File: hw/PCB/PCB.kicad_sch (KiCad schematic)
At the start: 208 parts, among them IC1 SN74HC251PWR, IC2 SN74LV138APWR, IC3 SN74HC251PWR, K1 KEYSW, K10 KEYSW, K11 KEYSW, K12 KEYSW, K13 KEYSW, K14 KEYSW, K16 KEYSW, K17 KEYSW, K18 KEYSW, K19 KEYSW, K2 KEYSW, K20 KEYSW, K21 KEYSW, K22 KEYSW, K23 KEYSW, K24 KEYSW, K25 KEYSW, K26 KEYSW, K27 KEYSW, K28 KEYSW, K29 KEYSW, K3 KEYSW, K31 KEYSW, K32 KEYSW, K33 KEYSW, K34 KEYSW, K35 KEYSW, K36 KEYSW, K37 KEYSW, K38 KEYSW, K39 KEYSW, K4 KEYSW, K40 KEYSW, K41 KEYSW, K42 KEYSW, K43 KEYSW, K44 KEYSW, K46 KEYSW, K47 KEYSW, K48 KEYSW, K49 KEYSW, K5 KEYSW, K50 KEYSW, K51 KEYSW, K52 KEYSW, K53 KEYSW, K54 KEYSW, K55 KEYSW, K56 KEYSW, K57 KEYSW, K58 KEYSW, K59 KEYSW, K6 KEYSW, K61 KEYSW, K62 KEYSW, K63 KEYSW, K64 KEYSW, K65 KEYSW, K66 KEYSW, K67 KEYSW, K68 KEYSW, K69 KEYSW, K7 KEYSW, K8 KEYSW, K9 KEYSW, U1 TXB0108DQSR, U6 STM32L552ZETxQ

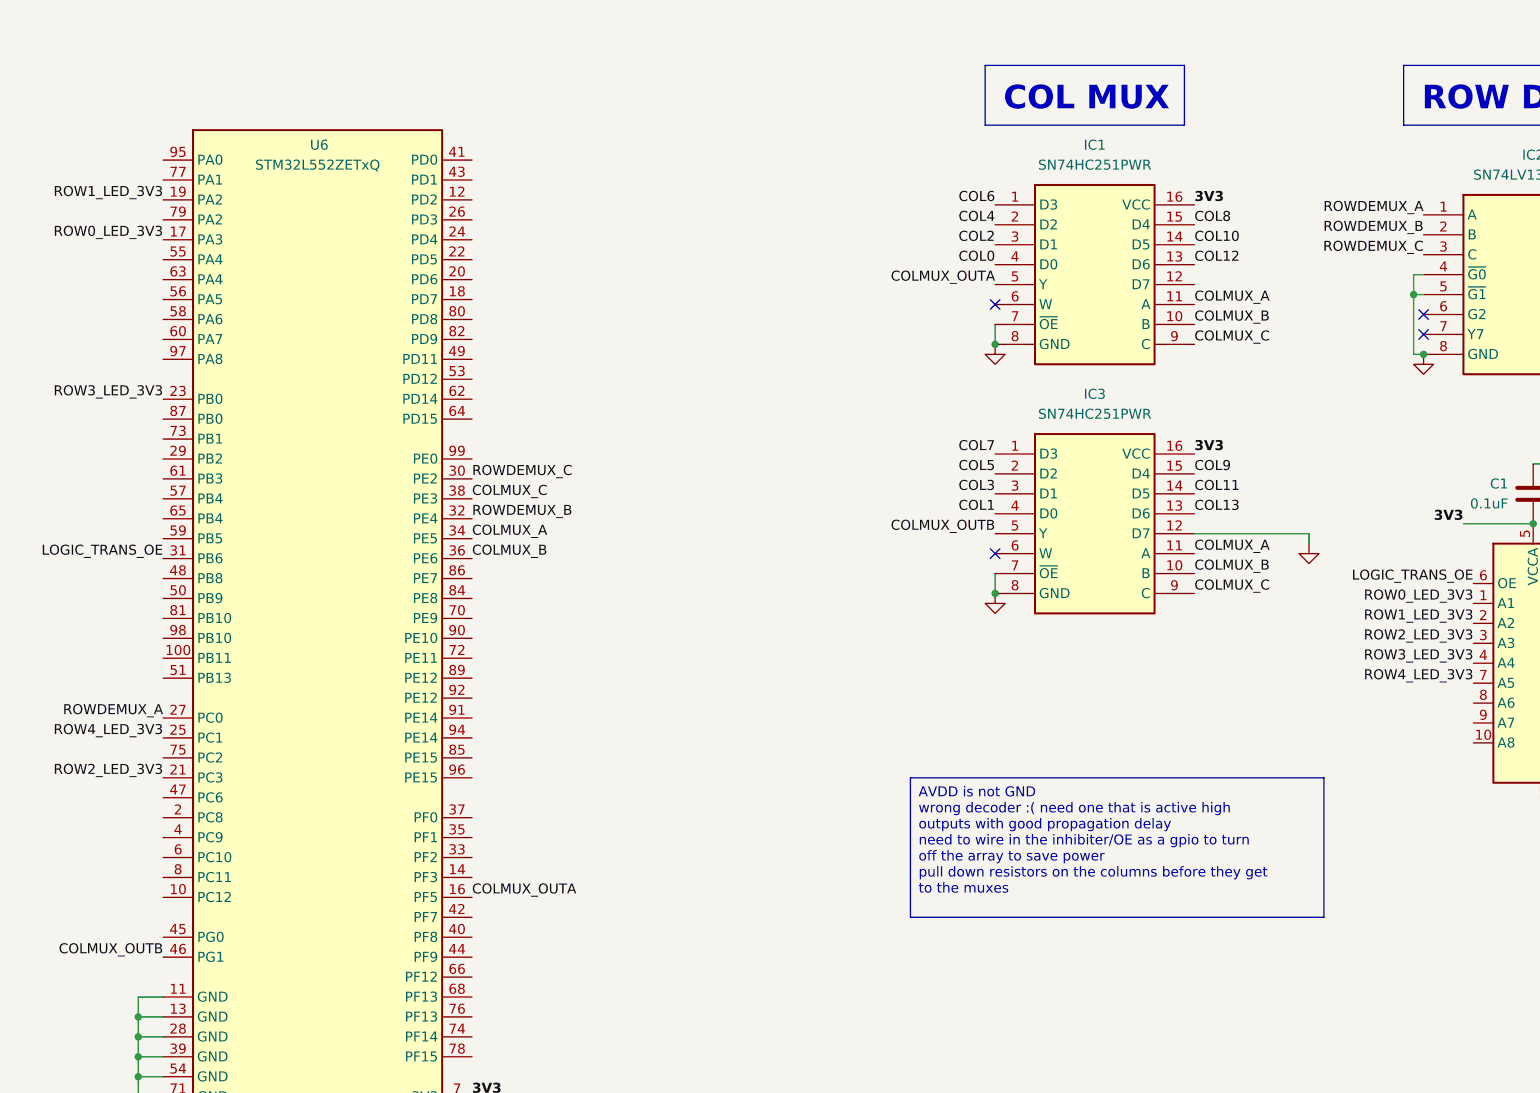
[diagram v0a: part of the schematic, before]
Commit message: The LEDs work!!
LEDs use DMA PWM to generate their bit encoding scheme
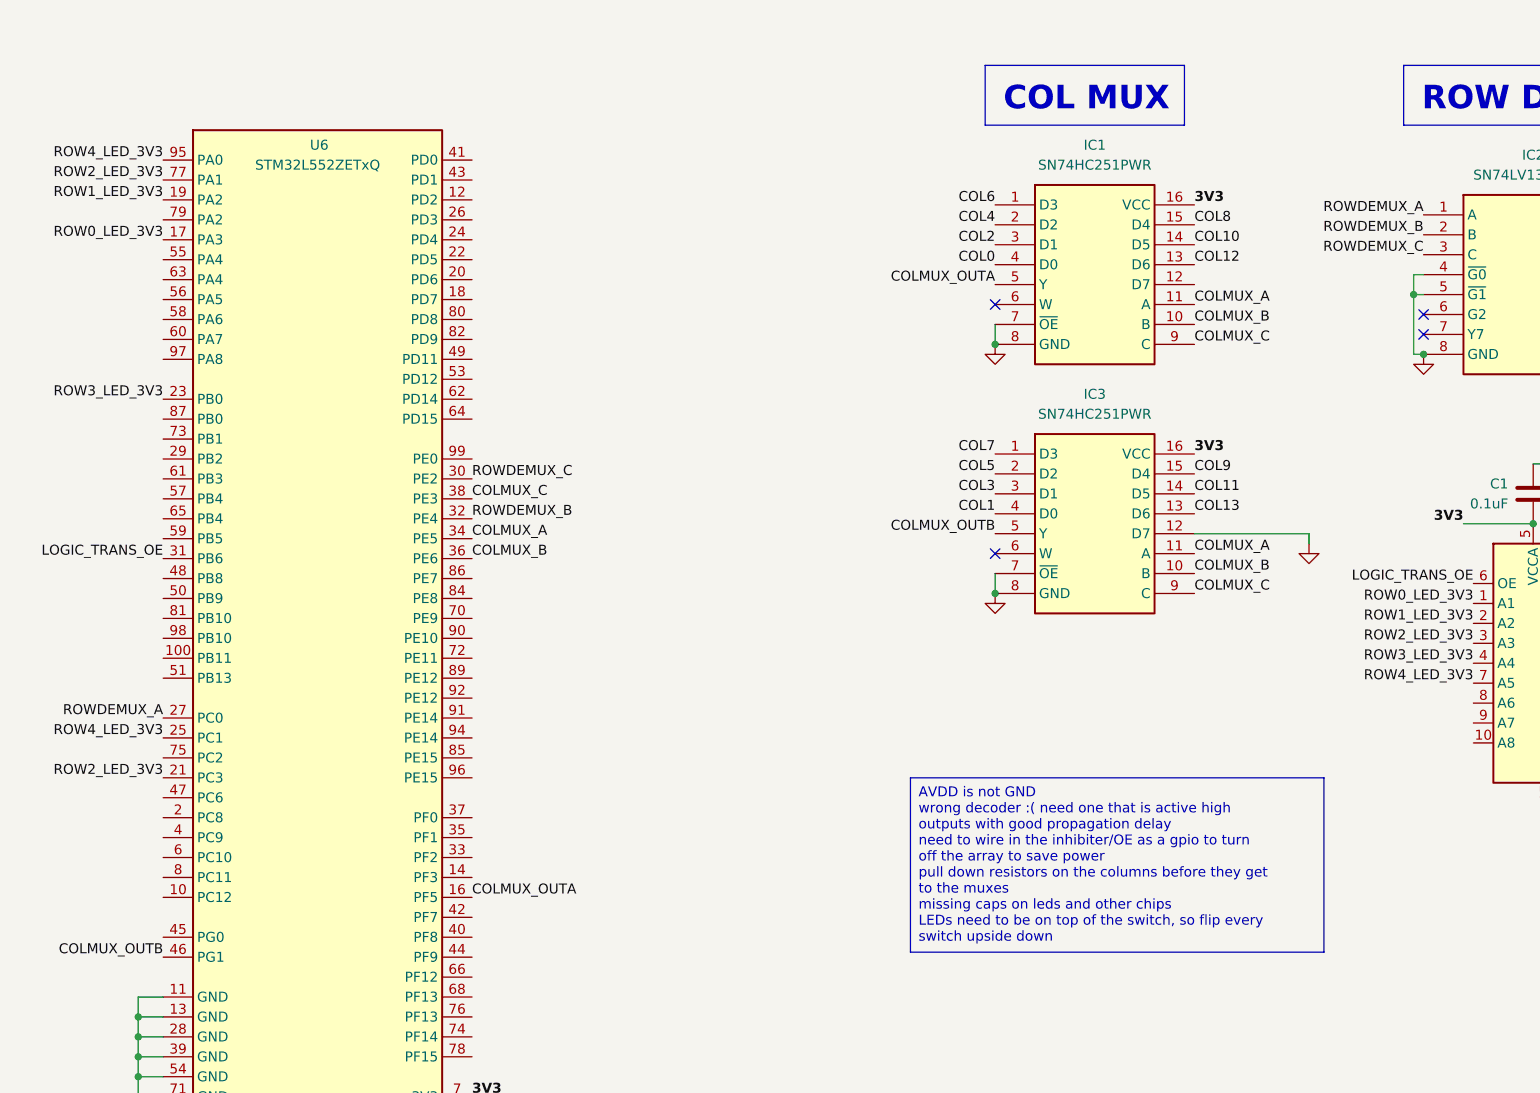
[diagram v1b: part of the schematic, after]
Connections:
- net ROW2_LED_3V3: now also U6.77 (PA1)
- net ROW4_LED_3V3: now also U6.95 (PA0)
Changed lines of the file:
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@@
     (effects (font (size 5 5) (thickness 0.254) bold (color 0 4 255 1)) (justify left top))
   )
-  (text_box "AVDD is not GND\nwrong decoder :( need one that is active high outputs with good propagation delay\nneed to wire in the inhibiter/OE as a gpio to turn off the array to save power\npull down resistors on the columns before they get to the muxes"
-    (at 156.21 182.245 0) (size 52.705 17.78)
+  (text_box "AVDD is not GND\nwrong decoder :( need one that is active high outputs with good propagation delay\nneed to wire in the inhibiter/OE as a gpio to turn off the array to save power\npull down resistors on the columns before they get to the muxes\nmissing caps on leds and other chips\nLEDs need to be on top of the switch, so flip every switch upside down"
+    (at 156.21 182.245 0) (size 52.705 22.225)
     (stroke (width 0) (type default))
     (fill (type none))
@@
     (effects (font (size 1.27 1.27)) (justify right bottom))
   )
+  (label "ROW4_LED_3V3" (at 60.96 103.505 180) (fields_autoplaced)
+    (effects (font (size 1.27 1.27)) (justify right bottom))
+  )
   (label "COL4" (at 167.005 111.76 180) (fields_autoplaced)
     (effects (font (size 1.27 1.27)) (justify right bottom))
@@
     (effects (font (size 1.27 1.27)) (justify left bottom))
   )
+  (label "ROW2_LED_3V3" (at 60.96 106.045 180) (fields_autoplaced)
+    (effects (font (size 1.27 1.27)) (justify right bottom))
+  )
   (label "ROW2_LED_3V3" (at 60.96 182.245 180) (fields_autoplaced)

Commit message: Schematic Updates
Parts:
- removed IC1: SN74HC251PWR, SN74HC251PWR:SOP65P640X120-16N, symbol SN74HC251PWR:SN74HC251PWR
- removed IC2: SN74LV138APWR, SN74LV138APWR:SOP65P640X120-16N, symbol SN74LV138APWR:SN74LV138APWR
- removed IC3: SN74HC251PWR, SN74LV138APWR:SOP65P640X120-16N, symbol SN74HC251PWR:SN74HC251PWR
- removed JP1, JP2, JP3, JP4, JP5, JP6: SolderJumper_2_Bridged, Jumper:SolderJumper-2_P1.3mm_Bridged_RoundedPad1.0x1.5mm, symbol Jumper:SolderJumper_2_Bridged
- removed LED69: WS2812B, Keebio-Parts.pretty-master:SK6812-MINI-E, symbol LED:WS2812B
- removed U1: TXB0108DQSR, Package_SON:USON-20_2x4mm_P0.4mm, symbol Logic_LevelTranslator:TXB0108DQSR
- removed U6: STM32L552ZETxQ, STZio:STZio, symbol STZio:STM32L552ZETxQ_Zio
- added 1: ~, symbol PCB-altium-import:root_0_Battery_pack_NTC
- added 1: ~, symbol PCB-altium-import:root_0_nPM1300_QEAA
- added C10, C12, C19, C20, C21, C22, C23, C24, C25, C26, C27, C28, C29, C3, C30, C31, C32, C33, C34, C35, C36, C37, C38, C39, C4, C40, C41, C42, C43, C44, C45, C46, C47, C48, C49, C5, C50, C51, C52, C53, C54, C55, C56, C57, C58, C59, C6, C60, C61, C62, C63, C64, C65, C66, C67, C68, C69, C7, C70, C71, C72, C73, C74, C8, C9: 100nF, symbol Device:C
- added C11: 2.2uF, symbol Device:C
- added C13: 1uF, symbol Device:C
- added C16: 10uF, symbol Device:C
- added D15: D, Diode_SMD:D_SOD-123, symbol Device:D
- added D30: PRTR5V0U2X, Package_TO_SOT_SMD:SOT-143, symbol Power_Protection:PRTR5V0U2X
- added J1: USB_C_Receptacle_USB2.0, Connector_USB:USB3_A_Molex_48393-001, symbol Connector:USB_C_Receptacle_USB2.0
- added J2: Adafruit TFT, symbol Connector_Generic:Conn_01x11
- added K15: KEYSW, MX_Hotswap:MX-Hotswap-1.25U, symbol keyboard_parts:KEYSW
- added L0603G: ~, symbol Device:LED
- added L0603R, L0603Y: LED, symbol Device:LED
- added L1, L2: 2.2uH, symbol Device:L
- added LED15, LED30: WS2812B, Keebio-Parts.pretty-master:SK6812-MINI-E, symbol LED:WS2812B
- added R1: 47K, symbol Device:R
- added R2: 250K, symbol Device:R
- added SW1: SW_Push, symbol Switch:SW_Push
- added U1: nRF52840, Package_DFN_QFN:Nordic_AQFN-73-1EP_7x7mm_P0.5mm, symbol MCU_Nordic:nRF52840
- added U2: MS88SF2, MS88SF2:XCVR_MS88SF2, symbol MS88SF2:MS88SF2
- added U3, U4: 74HC595, symbol 74xx:74HC595
- C1, C2: value 0.1uF -> 100nF; footprint Capacitor_SMD:C_0603_1608Metric_Pad1.08x0.95mm_HandSolder -> (none)
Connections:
- net 3V3 is gone; now on net GND: C1.2
- net ROW1_LED_5V is gone; now on an unnamed net: LED29.4 (DIN)
- net ROW2_LED_5V is gone; now on an unnamed net: LED44.4 (DIN)
- net 5V: now also C1.1, C2.1, LED1.1 (VDD), LED10.1 (VDD), LED11.1 (VDD), LED12.1 (VDD), LED13.1 (VDD), LED14.1 (VDD), LED16.1 (VDD), LED17.1 (VDD), LED18.1 (VDD), LED19.1 (VDD), LED2.1 (VDD), LED20.1 (VDD), LED21.1 (VDD), LED22.1 (VDD), LED23.1 (VDD), LED24.1 (VDD), LED25.1 (VDD), LED26.1 (VDD), LED27.1 (VDD), LED28.1 (VDD), LED29.1 (VDD), LED3.1 (VDD), LED31.1 (VDD), LED32.1 (VDD), LED33.1 (VDD), LED34.1 (VDD), LED35.1 (VDD), LED36.1 (VDD), LED37.1 (VDD), LED38.1 (VDD), LED39.1 (VDD), LED4.1 (VDD), LED40.1 (VDD), LED41.1 (VDD), LED42.1 (VDD), LED43.1 (VDD), LED44.1 (VDD), LED46.1 (VDD), LED47.1 (VDD), LED48.1 (VDD), LED49.1 (VDD), LED5.1 (VDD), LED50.1 (VDD), LED51.1 (VDD), LED52.1 (VDD), LED53.1 (VDD), LED54.1 (VDD), LED55.1 (VDD), LED56.1 (VDD), LED57.1 (VDD), LED58.1 (VDD), LED59.1 (VDD), LED6.1 (VDD), LED61.1 (VDD), LED62.1 (VDD), LED63.1 (VDD), LED64.1 (VDD), LED65.1 (VDD), LED66.1 (VDD), LED67.1 (VDD), LED68.1 (VDD), LED7.1 (VDD), LED8.1 (VDD), LED9.1 (VDD), C10.1, C19.1, C20.1, C21.1, C22.1, C23.1, C24.1, C25.1, C26.1, C27.1, C28.1, C29.1, C3.1, C30.1, C31.1, C32.1, C33.1, C34.1, C35.1, C36.1, C37.1, C38.1, C39.1, C4.1, C40.1, C41.1, C42.1, C43.1, C44.1, C45.1, C46.1, C47.1, C48.1, C49.1, C5.1, C50.1, C51.1, C52.1, C53.1, C54.1, C55.1, C56.1, C57.1, C58.1, C59.1, C6.1, C60.1, C61.1, C62.1, C63.1, C64.1, C65.1, C66.1, C67.1, C68.1, C69.1, C7.1, C70.1, C71.1, C72.1, C73.1, C74.1, C8.1, C9.1, LED15.1 (VDD), LED30.1 (VDD)
- net COL0: now also U3.15 (QA)
- net COL1: now also U3.1 (QB)
- net COL10: now also U4.2 (QC)
- net COL11: now also U4.3 (QD)
- net COL12: now also U4.4 (QE)
- net COL13: now also U4.5 (QF)
- net COL2: now also U3.2 (QC)
- net COL3: now also U3.3 (QD)
- net COL4: now also U3.4 (QE)
- net COL5: now also U3.5 (QF)
- net COL6: now also U3.6 (QG)
- net COL7: now also U3.7 (QH)
- net COL8: now also K15.1, U4.15 (QA)
- net COL9: now also U4.1 (QB)
- net GND: now also C2.2, 1.2 (PVSS1), 1.28 (LSIN1/VINLDO1), 1.29 (LSOUT1/VOUTLDO1), 1.30 (LSIN2/VINLDO2), 1.31 (LSOUT2/VOUTLDO2), 1.33 (AVSS), 1.6 (PVSS2), C10.2, C11.1, C12.2, C13.2, C16.2, C19.2, C20.2, C21.2, C22.2, C23.2, C24.2, C25.2, C26.2, C27.2, C28.2, C29.2, C3.2, C30.2, C31.2, C32.2, C33.2, C34.2, C35.2, C36.2, C37.2, C38.2, C39.2, C4.2, C40.2, C41.2, C42.2, C43.2, C44.2, C45.2, C46.2, C47.2, C48.2, C49.2, C5.2, C50.2, C51.2, C52.2, C53.2, C54.2, C55.2, C56.2, C57.2, C58.2, C59.2, C6.2, C60.2, C61.2, C62.2, C63.2, C64.2, C65.2, C66.2, C67.2, C68.2, C69.2, C7.2, C70.2, C71.2, C72.2, C73.2, C74.2, C8.2, C9.2, D30.1 (GND), J1.A1 (GND), J1.A12 (GND), J1.B1 (GND), J1.B12 (GND), J1.S1 (SHIELD), J2.3 (Pin_3), LED15.3 (VSS), LED30.3 (VSS), R1.2, R2.2, SW1.1, U3.13 (~{OE}), U4.13 (~{OE}); no longer C1.1, C2.1
- net ROW0: now also D1.1 (K), D10.1 (K), D11.1 (K), D12.1 (K), D13.1 (K), D14.1 (K), D2.1 (K), D3.1 (K), D4.1 (K), D5.1 (K), D6.1 (K), D7.1 (K), D8.1 (K), D9.1 (K); no longer D1.2 (A), D10.2 (A), D11.2 (A), D12.2 (A), D13.2 (A), D14.2 (A), D2.2 (A), D3.2 (A), D4.2 (A), D5.2 (A), D6.2 (A), D7.2 (A), D8.2 (A), D9.2 (A)
- net ROW1: now also D16.1 (K), D17.1 (K), D18.1 (K), D19.1 (K), D20.1 (K), D21.1 (K), D22.1 (K), D23.1 (K), D24.1 (K), D25.1 (K), D26.1 (K), D27.1 (K), D28.1 (K), D29.1 (K); no longer D16.2 (A), D17.2 (A), D18.2 (A), D19.2 (A), D20.2 (A), D21.2 (A), D22.2 (A), D23.2 (A), D24.2 (A), D25.2 (A), D26.2 (A), D27.2 (A), D28.2 (A), D29.2 (A)
- net ROW2: now also D31.1 (K), D32.1 (K), D33.1 (K), D34.1 (K), D35.1 (K), D36.1 (K), D37.1 (K), D38.1 (K), D39.1 (K), D40.1 (K), D41.1 (K), D42.1 (K), D43.1 (K), D44.1 (K); no longer D31.2 (A), D32.2 (A), D33.2 (A), D34.2 (A), D35.2 (A), D36.2 (A), D37.2 (A), D38.2 (A), D39.2 (A), D40.2 (A), D41.2 (A), D42.2 (A), D43.2 (A), D44.2 (A)
- net ROW3: now also D46.1 (K), D47.1 (K), D48.1 (K), D49.1 (K), D50.1 (K), D51.1 (K), D52.1 (K), D53.1 (K), D54.1 (K), D55.1 (K), D56.1 (K), D57.1 (K), D58.1 (K), D59.1 (K); no longer D46.2 (A), D47.2 (A), D48.2 (A), D49.2 (A), D50.2 (A), D51.2 (A), D52.2 (A), D53.2 (A), D54.2 (A), D55.2 (A), D56.2 (A), D57.2 (A), D58.2 (A), D59.2 (A)
- net ROW4: now also D61.1 (K), D62.1 (K), D63.1 (K), D64.1 (K), D65.1 (K), D66.1 (K), D67.1 (K), D68.1 (K), D69.1 (K), D15.1 (K); no longer D61.2 (A), D62.2 (A), D63.2 (A), D64.2 (A), D65.2 (A), D66.2 (A), D67.2 (A), D68.2 (A), D69.2 (A)
- net at LED34.2 (DOUT): now also LED35.4 (DIN); no longer LED33.4 (DIN)
- net at LED34.4 (DIN): now also LED33.2 (DOUT); no longer LED35.2 (DOUT)
- net at K43.2: now also D43.2 (A); no longer D43.1 (K)
- net at K4.2: now also D4.2 (A); no longer D4.1 (K)
- net at K19.2: now also D19.2 (A); no longer D19.1 (K)
- net at K68.2: now also D68.2 (A); no longer D68.1 (K)
- net at K66.2: now also D66.2 (A); no longer D66.1 (K)
- net at LED66.2 (DOUT): now also LED67.4 (DIN); no longer LED65.4 (DIN)
- net at LED66.4 (DIN): now also LED65.2 (DOUT); no longer LED67.2 (DOUT)
- net at K7.2: now also D7.2 (A); no longer D7.1 (K)
- net at LED10.2 (DOUT): now also LED11.4 (DIN); no longer LED9.4 (DIN)
- net at LED10.4 (DIN): now also LED9.2 (DOUT); no longer LED11.2 (DOUT)
- net at K5.2: now also D5.2 (A); no longer D5.1 (K)
- net at K6.2: now also D6.2 (A); no longer D6.1 (K)
- net at K53.2: now also D53.2 (A); no longer D53.1 (K)
- net at K3.2: now also D3.2 (A); no longer D3.1 (K)
- net at LED44.2 (DOUT): no longer LED43.4 (DIN)
- net at K35.2: now also D35.2 (A); no longer D35.1 (K)
- net at LED5.2 (DOUT): now also LED6.4 (DIN); no longer LED4.4 (DIN)
- net at LED5.4 (DIN): now also LED4.2 (DOUT); no longer LED6.2 (DOUT)
- net at K63.2: now also D63.2 (A); no longer D63.1 (K)
- net at K44.2: now also D44.2 (A); no longer D44.1 (K)
- net at K50.2: now also D50.2 (A); no longer D50.1 (K)
- net at K20.2: now also D20.2 (A); no longer D20.1 (K)
- net at K67.2: now also D67.2 (A); no longer D67.1 (K)
- net at K41.2: now also D41.2 (A); no longer D41.1 (K)
- net at K28.2: now also D28.2 (A); no longer D28.1 (K)
- net at LED37.2 (DOUT): now also LED38.4 (DIN); no longer LED36.4 (DIN)
- net at LED37.4 (DIN): now also LED36.2 (DOUT); no longer LED38.2 (DOUT)
- net at K26.2: now also D26.2 (A); no longer D26.1 (K)
- net at K37.2: now also D37.2 (A); no longer D37.1 (K)
- net at K17.2: now also D17.2 (A); no longer D17.1 (K)
- net at LED63.2 (DOUT): now also LED64.4 (DIN); no longer LED62.4 (DIN)
- net at LED63.4 (DIN): now also LED62.2 (DOUT); no longer LED64.2 (DOUT)
- net at K31.2: now also D31.2 (A); no longer D31.1 (K)
- net at K32.2: now also D32.2 (A); no longer D32.1 (K)
- net at K33.2: now also D33.2 (A); no longer D33.1 (K)
- net at LED41.2 (DOUT): now also LED42.4 (DIN); no longer LED40.4 (DIN)
- net at LED41.4 (DIN): now also LED40.2 (DOUT); no longer LED42.2 (DOUT)
- net at LED31.2 (DOUT): now also LED32.4 (DIN)
- net at LED31.4 (DIN): now also LED46.2 (DOUT); no longer LED32.2 (DOUT)
- net at K59.2: now also D59.2 (A); no longer D59.1 (K)
- net at K18.2: now also D18.2 (A); no longer D18.1 (K)
- net at LED16.2 (DOUT): now also LED1.4 (DIN)
- net at K42.2: now also D42.2 (A); no longer D42.1 (K)
- net at K25.2: now also D25.2 (A); no longer D25.1 (K)
- net at K47.2: now also D47.2 (A); no longer D47.1 (K)
- net at K52.2: now also D52.2 (A); no longer D52.1 (K)
- net at K55.2: now also D55.2 (A); no longer D55.1 (K)
- net at K36.2: now also D36.2 (A); no longer D36.1 (K)
- net at K12.2: now also D12.2 (A); no longer D12.1 (K)
- net at K40.2: now also D40.2 (A); no longer D40.1 (K)
- net at K8.2: now also D8.2 (A); no longer D8.1 (K)
- net at K49.2: now also D49.2 (A); no longer D49.1 (K)
- net at LED39.2 (DOUT): now also LED40.4 (DIN); no longer LED38.4 (DIN)
- net at LED39.4 (DIN): now also LED38.2 (DOUT); no longer LED40.2 (DOUT)
- net at K11.2: now also D11.2 (A); no longer D11.1 (K)
- net at LED3.2 (DOUT): now also LED4.4 (DIN); no longer LED2.4 (DIN)
- net at LED3.4 (DIN): now also LED2.2 (DOUT); no longer LED4.2 (DOUT)
- net at K29.2: now also D29.2 (A); no longer D29.1 (K)
- net at K61.2: now also D61.2 (A); no longer D61.1 (K)
- net at K48.2: now also D48.2 (A); no longer D48.1 (K)
- net at LED43.2 (DOUT): no longer LED42.4 (DIN)
- net at K56.2: now also D56.2 (A); no longer D56.1 (K)
- net at K64.2: now also D64.2 (A); no longer D64.1 (K)
- net at K13.2: now also D13.2 (A); no longer D13.1 (K)
- net at K69.2: now also D69.2 (A); no longer D69.1 (K)
- net at K1.2: now also D1.2 (A); no longer D1.1 (K)
- net at LED8.2 (DOUT): now also LED9.4 (DIN); no longer LED7.4 (DIN)
- net at LED8.4 (DIN): now also LED7.2 (DOUT); no longer LED9.2 (DOUT)
- net at LED61.4 (DIN): no longer LED62.2 (DOUT)
- net at LED12.2 (DOUT): now also LED13.4 (DIN); no longer LED11.4 (DIN)
- net at LED12.4 (DIN): now also LED11.2 (DOUT); no longer LED13.2 (DOUT)
- net at K16.2: now also D16.2 (A); no longer D16.1 (K)
- net at K14.2: now also D14.2 (A); no longer D14.1 (K)
- net at K27.2: now also D27.2 (A); no longer D27.1 (K)
- net at K62.2: now also D62.2 (A); no longer D62.1 (K)
- net at K34.2: now also D34.2 (A); no longer D34.1 (K)
- net at K46.2: now also D46.2 (A); no longer D46.1 (K)
- net at K10.2: now also D10.2 (A); no longer D10.1 (K)
- net at K51.2: now also D51.2 (A); no longer D51.1 (K)
- net at LED61.2 (DOUT): now also LED62.4 (DIN)
- net at K54.2: now also D54.2 (A); no longer D54.1 (K)
- net at LED68.2 (DOUT): now also LED15.4 (DIN); no longer LED67.4 (DIN)
- net at K65.2: now also D65.2 (A); no longer D65.1 (K)
- net at LED1.2 (DOUT): now also LED2.4 (DIN)
- net at K23.2: now also D23.2 (A); no longer D23.1 (K)
- net at K2.2: now also D2.2 (A); no longer D2.1 (K)
- net at LED14.2 (DOUT): no longer LED13.4 (DIN)
- net at K57.2: now also D57.2 (A); no longer D57.1 (K)
- net at LED68.4 (DIN): now also LED67.2 (DOUT)
- net at K58.2: now also D58.2 (A); no longer D58.1 (K)
- net at K38.2: now also D38.2 (A); no longer D38.1 (K)
- net at K22.2: now also D22.2 (A); no longer D22.1 (K)
- net at K21.2: now also D21.2 (A); no longer D21.1 (K)
- net at K39.2: now also D39.2 (A); no longer D39.1 (K)
- net at K24.2: now also D24.2 (A); no longer D24.1 (K)
- net at K9.2: now also D9.2 (A); no longer D9.1 (K)
- net ROW0_LED_5V: no longer names the net of LED14.4 (DIN)
- net ROW0_LED_5V: now also LED13.2 (DOUT)
- net ROW3_LED_5V: no longer names the net of LED59.4 (DIN)
- net ROW3_LED_5V: now also LED30.2 (DOUT)
- new net: 1.21 (VBUS), D30.4 (VCC), J1.A4 (VBUS), J1.A9 (VBUS), J1.B4 (VBUS), J1.B9 (VBUS)
- new net: D15.2 (A), K15.2
- new net: U3.9 (QH'), U4.14 (SER)
- new net: LED32.2 (DOUT), LED33.4 (DIN)
- new net: U1.A22 (VDD), U1.AD14 (VDD), U1.AD23 (VDD), U1.B1 (VDD), U1.W1 (VDD)
- new net: U1.B7 (VSS), U1.EP (VSS)
- new net: LED35.2 (DOUT), LED36.4 (DIN)
- new net: LED15.2 (DOUT), LED30.4 (DIN)
- new net: 1.3 (SW1), L1.2
- new net: LED42.2 (DOUT), LED43.4 (DIN)
- new net: 1.18 (NTC), 1.2 (NTC)
- new net: 1.19 (VBAT), 1.3 (V+), C11.2
- new net: U2.1 (GND), U2.13 (GND)
- new net: 1.5 (SW2), L2.2
- new net: 1.12 (VDDIO), C12.1
- new net: LED6.2 (DOUT), LED7.4 (DIN)
- new net: 1.16 (VSET2), R2.1
- new net: 1.25 (LED0), L0603G.1 (K)
- new net: 1.17 (VSET1), R1.1
- new net: LED64.2 (DOUT), LED65.4 (DIN)
- new net: 1.23 (CC1), J1.A5 (CC1)
- new net: 1.24 (CC2), J1.B5 (CC2)
- new net: 1.26 (LED1), L0603Y.1 (K)
- new net: 1.27 (LED2), L0603R.1 (K)
- new net 3.3V: J2.1 (Pin_1)
- new net COL14: U4.6 (QG)
- new net COL_CS: U3.12 (RCLK), U4.12 (RCLK)
- new net COL_MOSI: U3.14 (SER)
- new net COL_SCK: U3.11 (SRCLK), U4.11 (SRCLK)
- new net D+: D30.2 (I/O1), J1.A6 (D+), J1.B6 (D+)
- new net D-: D30.3 (I/O2), J1.A7 (D-), J1.B7 (D-)
- new net NPM_GPIO2: 1.9 (GPIO2)
- new net NPM_GPIO3: 1.10 (GPIO3)
- new net NPM_GPIO4: 1.11 (GPIO4)
- new net NPM_INT: 1.8 (GPIO1)
- new net NPM_SCL: 1.14 (SCL)
- new net NPM_SDA: 1.13 (SDA)
- new net RESET: 1.7 (GPIO0), SW1.2
- new net TFT_CS: J2.7 (Pin_7)
- new net TFT_DC: J2.9 (Pin_9)
- new net TFT_LITE: J2.11 (Pin_11)
- new net TFT_MOSI: J2.6 (Pin_6)
- new net TFT_RESET: J2.8 (Pin_8)
- new net TFT_SCK: J2.4 (Pin_4)
- new net VBUS: U2.15 (VDDH)
- new net VBUSOUT: 1.22 (VBUSOUT), C13.1
- new net VCC: U3.10 (~{SRCLR}), U4.10 (~{SRCLR})
- new net VOUT1: 1.1 (VOUT1), L1.1
- new net VOUT2: 1.32 (VOUT2), L2.1
- new net VSYS: 1.20 (VSYS), 1.4 (PVDD), C16.1, L0603G.2 (A), L0603R.2 (A), L0603Y.2 (A)
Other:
- note added: "0Ω 0.0 V 4.7 kΩ 1.0 V 10 kΩ 1.2 V 22 kΩ 1.5 V 47 kΩ 1.8 V 68 kΩ 2.0 V 100 kΩ 2.2 V 150 kΩ 2.5 V 250-500 kΩ 2.7 V"
- note added: "0Ω 0.0 V 4.7 kΩ 1.8 V 10 kΩ 2.0 V 22 kΩ 2.2 V 47 kΩ 2.4 V 68 kΩ 2.5 V 100 kΩ 2.7 V 150 kΩ 3.0 V 250-500 kΩ 3.3 V"
- note added: "1.8V for nRF internal supply"
- note added: "EXTRA"
- note added: "These operate at VDD"
- note added: "VDDH will be the voltage of the external power supply. This power supply can be either 5V from USB or 3.7V LiPo. No extra power filtering circuitry is needed, just switching."
- note added: "VSET1"
- note added: "VSET2"
- note removed: "MENU"
- moved on the sheet: K1

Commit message: "finished" schematic with MinewSemi nRF52840 module
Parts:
- removed L0603G: ~, symbol Device:LED
- removed L0603R, L0603Y: LED, symbol Device:LED
- removed L1, L2: 2.2uH, symbol Device:L
- removed R1: 47K, symbol Device:R
- removed R2: 250K, symbol Device:R
- removed U1: nRF52840, Package_DFN_QFN:Nordic_AQFN-73-1EP_7x7mm_P0.5mm, symbol MCU_Nordic:nRF52840
- added C93: 1uF, Capacitor_SMD:C_0603_1608Metric, symbol Device:C
- added IC1: TXU0101DCKR, SOT65P210X110-6N, symbol TXU0101DCKR:TXU0101DCKR
- added IC2: W25Q64JVXGIQ_TR, W25Q64JVXGIQ_TR:SON80P400X400X50-9N, symbol W25Q64JVXGIQ_TR:W25Q64JVXGIQ_TR
- added J3: Conn_ARM_JTAG_SWD_10, Connector_PinHeader_1.27mm:PinHeader_2x05_P1.27mm_Vertical, symbol Connector:Conn_ARM_JTAG_SWD_10
- added SW2: RotaryEncoder_Switch, Roller Encoder:RollerEncoder_Panasonic_EVQWGD001, symbol Device:RotaryEncoder_Switch
- BT1: renamed from 1; footprint (none) -> Connector_JST:JST_GH_SM03B-GHS-TB_1x03-1MP_P1.25mm_Horizontal
- C1, C10, C11, C13, C16, C19, C2, C20, C21, C22, C23, C24, C25, C26, C27, C28, C29, C3, C30, C31, C32, C33, C34, C35, C36, C37, C38, C39, C4, C40, C41, C42, C43, C44, C45, C46, C47, C48, C49, C5, C50, C51, C52, C53, C54, C55, C56, C57, C58, C59, C6, C60, C61, C62, C63, C64, C65, C66, C67, C68, C69, C7, C70, C71, C72, C73, C74, C8, C9: footprint (none) -> Capacitor_SMD:C_0603_1608Metric
- C12: footprint (none) -> Capacitor_SMD:C_0201_0603Metric
- J1: footprint Connector_USB:USB3_A_Molex_48393-001 -> Adafruit-USB-C-Downstream-Breakout-master:Adafruit_USB_C_2.0
- J2: footprint (none) -> Adafruit:Adafruit_1.47_TFT_Round_Rect
- SW1: footprint (none) -> Button_Switch_SMD:SW_SPST_EVPBF
- U3, U4: footprint (none) -> Package_SO:TSSOP-16_4.4x5mm_P0.65mm
- U5: renamed from 1; footprint (none) -> nPM1300:nPM1300-QEAA
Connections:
- net 3.3V is gone; now on net VDD: J2.1 (Pin_1)
- net 5V is gone; now on net VSYS: C1.1, C10.1, C19.1, C2.1, C20.1, C21.1, C22.1, C23.1, C24.1, C25.1, C26.1, C27.1, C28.1, C29.1, C3.1, C30.1, C31.1, C32.1, C33.1, C34.1, C35.1, C36.1, C37.1, C38.1, C39.1, C4.1, C40.1, C41.1, C42.1, C43.1, C44.1, C45.1, C46.1, C47.1, C48.1, C49.1, C5.1, C50.1, C51.1, C52.1, C53.1, C54.1, C55.1, C56.1, C57.1, C58.1, C59.1, C6.1, C60.1, C61.1, C62.1, C63.1, C64.1, C65.1, C66.1, C67.1, C68.1, C69.1, C7.1, C70.1, C71.1, C72.1, C73.1, C74.1, C8.1, C9.1, LED1.1 (VDD), LED10.1 (VDD), LED11.1 (VDD), LED12.1 (VDD), LED13.1 (VDD), LED14.1 (VDD), LED15.1 (VDD), LED16.1 (VDD), LED17.1 (VDD), LED18.1 (VDD), LED19.1 (VDD), LED2.1 (VDD), LED20.1 (VDD), LED21.1 (VDD), LED22.1 (VDD), LED23.1 (VDD), LED24.1 (VDD), LED25.1 (VDD), LED26.1 (VDD), LED27.1 (VDD), LED28.1 (VDD), LED29.1 (VDD), LED3.1 (VDD), LED30.1 (VDD), LED31.1 (VDD), LED32.1 (VDD), LED33.1 (VDD), LED34.1 (VDD), LED35.1 (VDD), LED36.1 (VDD), LED37.1 (VDD), LED38.1 (VDD), LED39.1 (VDD), LED4.1 (VDD), LED40.1 (VDD), LED41.1 (VDD), LED42.1 (VDD), LED43.1 (VDD), LED44.1 (VDD), LED46.1 (VDD), LED47.1 (VDD), LED48.1 (VDD), LED49.1 (VDD), LED5.1 (VDD), LED50.1 (VDD), LED51.1 (VDD), LED52.1 (VDD), LED53.1 (VDD), LED54.1 (VDD), LED55.1 (VDD), LED56.1 (VDD), LED57.1 (VDD), LED58.1 (VDD), LED59.1 (VDD), LED6.1 (VDD), LED61.1 (VDD), LED62.1 (VDD), LED63.1 (VDD), LED64.1 (VDD), LED65.1 (VDD), LED66.1 (VDD), LED67.1 (VDD), LED68.1 (VDD), LED7.1 (VDD), LED8.1 (VDD), LED9.1 (VDD)
- net COL_CS is gone; now on net GND: U3.12 (RCLK), U4.12 (RCLK)
- net TFT_CS is gone; now on net GND: J2.7 (Pin_7)
- net VBUS is gone; now on net VSYS: U2.15 (VDDH)
- net VCC is gone; now on net VDD: U3.10 (~{SRCLR}), U4.10 (~{SRCLR})
- net VOUT1 is gone; now on net VSYS: U5.1 (VOUT1)
- net VOUT2 is gone; now on net VSYS: U5.32 (VOUT2)
- net COL_MOSI: now also U2.6 (P0.31)
- net COL_SCK: now also U2.24 (P1.00)
- net D+: now also U2.17 (D+)
- net D-: now also U2.16 (D-)
- net GND: now also BT1.1 (GND), U2.1 (GND), U2.13 (GND), U3.8 (GND), U4.8 (GND), U5.3 (SW1), U5.5 (SW2), C93.1, IC1.2 (GND), IC2.1 (~{CS}), IC2.4 (GND), IC2.9 (EP), J3.3 (GND), J3.5 (GND), J3.9 (GNDDetect), SW2.C, SW2.S1
- net ROW0: now also U2.3 (P1.15)
- net ROW1: now also U2.2 (P1.13)
- net ROW2: now also U2.22 (P0.22)
- net ROW3: now also U2.20 (P0.18/~{RESET})
- net ROW4: now also U2.12 (P0.12)
- net TFT_DC: now also U2.23 (P0.24)
- net TFT_LITE: now also U2.18 (P0.13)
- net TFT_MOSI: now also U2.21 (P0.20)
- net TFT_SCK: now also U2.19 (P0.15)
- net VSYS: now also IC1.5 (OE), IC1.6 (VCCB)
- net at D30.4 (VCC), J1.A4 (VBUS), J1.A9 (VBUS)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: now also C93.2
- net VDD: now reaches U3.16 (VCC)
- net VDD: now also C12.1, U2.14 (VDD), U4.16 (VCC), U5.12 (VDDIO), IC1.1 (VCCA), IC2.8 (VCC), J3.1 (VTref)
- net FLASH_IO3: now reaches U2.10 (P0.08)
- net FLASH_IO3: now also IC2.7 (~{HOLD_OR_}RESET_(IO3))
- net FLASH_SCK: now reaches U2.11 (P1.09)
- net FLASH_SCK: now also IC2.6 (CLK)
- net SWDIO: now reaches U2.25 (SWDIO)
- net SWDIO: now also J3.2 (SWDIO/TMS)
- net SWDCLK: now reaches U2.26 (SWCLK)
- net SWDCLK: now also J3.4 (SWDCLK/TCK)
- net ENC_A: now reaches U2.27 (P0.09/NFC1)
- net ENC_A: now also SW2.A
- net ENC_B: now reaches U2.28 (P0.10/NFC2)
- net ENC_B: now also SW2.B
- net LED_SERIAL: now reaches U2.4 (P0.02)
- net LED_SERIAL: now also IC1.3 (A)
- net ENC_SW: now reaches U2.5 (P0.29)
- net ENC_SW: now also SW2.S2
- net FLASH_IO0: now reaches U2.7 (P0.26)
- net FLASH_IO0: now also IC2.5 (DI_(IO0))
- net FLASH_IO1: now reaches U2.8 (P0.04)
- net FLASH_IO1: now also IC2.2 (DO_(IO1))
- net FLASH_IO2: now reaches U2.9 (P0.06)
- net FLASH_IO2: now also IC2.3 (~{WP_(IO2)})
- net at LED61.4 (DIN): now also IC1.4 (BY)
- net ~{RESET}: now reaches U5.15 (SHPHLD)
- net ~{RESET}: now also SW1.2, J3.10 (~{RESET})
- net COL14: no longer names the net of U4.6 (QG)
- net RESET: no longer names the net of U5.7 (GPIO0)
- net RESET: no longer SW1.2
- net TFT_RESET: no longer names the net of J2.8 (Pin_8)
- no-connect marks 6 -> 17
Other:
- note added: "Board should be powered through USB or battery for flash/debug"
- note added: "Drive column to row"
- note added: "Level shifter for VDD->VSYS translation"
- note added: "Pull-ups not needed MCU internals are low enough (13k)"
- note added: "Runs on VSYS (5V from VBUS or 3.7V from BAT) Caps are probably unnecessary but oh well"
- note added: "Takes VDD and LDOs it to 3.3V with level shifters on logic pins"
- note added: "This is for VBUS sensing only, cannot be loaded"
- note added: "Unregulated 5V or 3.7V (USB vs LiPo)"
- note added: "Use MCU pull-ups"
- note added: "nRF52840"
- note removed: "1.8V for nRF internal supply"
- note removed: "VDDH will be the voltage of the external power supply. This power supply can be either 5V from USB or 3.7V LiPo. No extra power filtering circuitry is needed, just switching."
- moved on the sheet: BT1, C11, C12, C13, C16, D30, J1, J2, U3, U4, U5

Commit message: Routing "done", holy moly
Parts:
- removed C47: 100nF, Capacitor_SMD:C_0603_1608Metric, symbol Device:C
- removed D44: D, Diode_SMD:D_SOD-123, symbol Device:D
- removed K44: KEYSW, MX_Hotswap:MX-Hotswap-1U, symbol keyboard_parts:KEYSW
- removed LED44: WS2812B, Keebio-Parts.pretty-master:SK6812-MINI-E, symbol LED:WS2812B
- removed SW1: SW_Push, Button_Switch_SMD:SW_SPST_EVPBF, symbol Switch:SW_Push
- added C14, C15, C17: 100nF, Capacitor_SMD:C_0603_1608Metric, symbol Device:C
- added J4: Conn_01x03_Pin, Connector_PinHeader_2.54mm:PinHeader_1x03_P2.54mm_Vertical, symbol Connector:Conn_01x03_Pin
- added R1, R2: 10K, Resistor_SMD:R_0603_1608Metric, symbol Device:R
- IC1: footprint SOT65P210X110-6N -> TXU0101DCKR:SOT65P210X110-6N
- K67, K68: footprint MX_Hotswap:MX-Hotswap-1.25U -> MX_Hotswap:MX-Hotswap-1U
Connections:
- net NPM_GPIO2 is gone; now on net ROW2: U5.9 (GPIO2)
- net NPM_GPIO3 is gone; now on net ROW1: U5.10 (GPIO3)
- net NPM_GPIO4 is gone; now on net ROW0: U5.11 (GPIO4)
- net NPM_INT is gone; now on net ROW3: U5.8 (GPIO1)
- net D+: now also J1.6 (D+); no longer J1.A6 (D+), J1.B6 (D+)
- net D-: now also J1.5 (D-); no longer J1.A7 (D-), J1.B7 (D-)
- net ENC_SW: now also U2.2 (P1.13); no longer U2.5 (P0.29)
- net GND: now also J1.1 (GND), C14.1, C15.1, C17.1; no longer J1.A1 (GND), J1.A12 (GND), J1.B1 (GND), J1.B12 (GND), J1.S1 (SHIELD), U3.12 (RCLK), U4.12 (RCLK)
- net LED_SERIAL: now also U2.22 (P0.22); no longer U2.4 (P0.02)
- net NPM_SCL: now also U2.12 (P0.12), R1.1
- net NPM_SDA: now also U2.18 (P0.13), R2.1
- net ROW0: no longer U2.3 (P1.15)
- net ROW1: no longer U2.2 (P1.13)
- net ROW2: no longer U2.22 (P0.22)
- net ROW3: no longer U2.20 (P0.18/~{RESET})
- net ROW4: now also U5.7 (GPIO0); no longer U2.12 (P0.12)
- net TFT_LITE: now also U2.3 (P1.15); no longer U2.18 (P0.13)
- net VDD: now also C14.2, C17.2, R1.2, R2.2
- net VSYS: now also C15.2, J4.2 (Pin_2)
- net ~{RESET}: now also U2.20 (P0.18/~{RESET}); no longer U5.15 (SHPHLD)
- net at LED29.4 (DIN): now also LED43.2 (DOUT)
- net VBAT: now reaches BT1.3 (V+), C11.2, U5.19 (VBAT)
- net VBAT: now also J4.3 (Pin_3)
- net at U5.23 (CC1): now also J1.4 (CC1); no longer J1.A5 (CC1)
- net at U5.24 (CC2): now also J1.8 (CC2); no longer J1.B5 (CC2)
- new net COL_RSCK: U2.5 (P0.29), U3.12 (RCLK), U4.12 (RCLK)
- new net VBUS: C93.2, D30.4 (VCC), J1.2 (VBUS), J4.1 (Pin_1), U5.21 (VBUS)
- no-connect marks 17 -> 19
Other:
- note added: "confirm npm1300 gpios work as expected MAKE SUPER SURE THE USB TRACES ARE KOSHER"
- note added: "to bypass npm1300 if needed"

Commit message: 12/31 Fab Submission
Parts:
- D1, D10, D11, D12, D13, D14, D15, D16, D17, D18, D19, D2, D20, D21, D22, D23, D24, D25, D26, D27, D28, D29, D3, D31, D32, D33, D34, D35, D36, D37, D38, D39, D4, D40, D41, D42, D43, D46, D47, D48, D49, D5, D50, D51, D52, D53, D54, D55, D56, D57, D58, D59, D6, D61, D62, D63, D64, D65, D66, D67, D68, D69, D7, D8, D9: value D -> 1N4448W
- LED1, LED10, LED11, LED12, LED13, LED14, LED15, LED16, LED17, LED18, LED19, LED2, LED20, LED21, LED22, LED23, LED24, LED25, LED26, LED27, LED28, LED29, LED3, LED30, LED31, LED32, LED33, LED34, LED35, LED36, LED37, LED38, LED39, LED4, LED40, LED41, LED42, LED43, LED46, LED47, LED48, LED49, LED5, LED50, LED51, LED52, LED53, LED54, LED55, LED56, LED57, LED58, LED59, LED6, LED61, LED62, LED63, LED64, LED65, LED66, LED67, LED68, LED7, LED8, LED9: value WS2812B -> SK6812-MINI-E
- U2: value MS88SF2 -> nRF52840-MS88SF2
- U5: value ~ -> nPM1300-QEAA
